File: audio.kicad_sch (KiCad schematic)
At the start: 100 parts, among them CN1 LEFT_JOY, CN2 RIGHT_JOY, CN3 RIGHT, CN4 LEFT, Q301 2N3906, Q321 MPF102, Q331 MPF102, Q921 MMBFJ113, Q931 MMBFJ113, U14 LF347, U15 74LS157, U3 PAULA, U38 MC1488, U90 DT1042, U91 DT1042, U92 DT1042, U93 DT1042

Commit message: DRAM chips replaced with SIMM module
Added logic to decode 2MB chip + 1.5MB slow
Rewired trapdoor slot
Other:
- title: Rämixx500 -> Rämixx500_max
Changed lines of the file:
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@@
 	(paper "A3")
 	(title_block
-		(title "Rämixx500")
-		(date "2021-05-22")
-		(rev "1")
+		(title "Rämixx500_max")
+		(date "2026-03-13")
+		(rev "2")
 		(company "SukkoPera")
 		(comment 1 "PAULA PREFERS THE TRADITIONAL MODES")

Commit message: removed ESD diodes
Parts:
- removed U90, U91, U92, U93: DT1042, Raemixx500:TSOP-6_Handsolder, symbol DT1042:DT1042
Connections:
- no-connect marks 2 -> 0
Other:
- note removed: "EXTRA TVS DIODES FOR ESD PROTECTION"

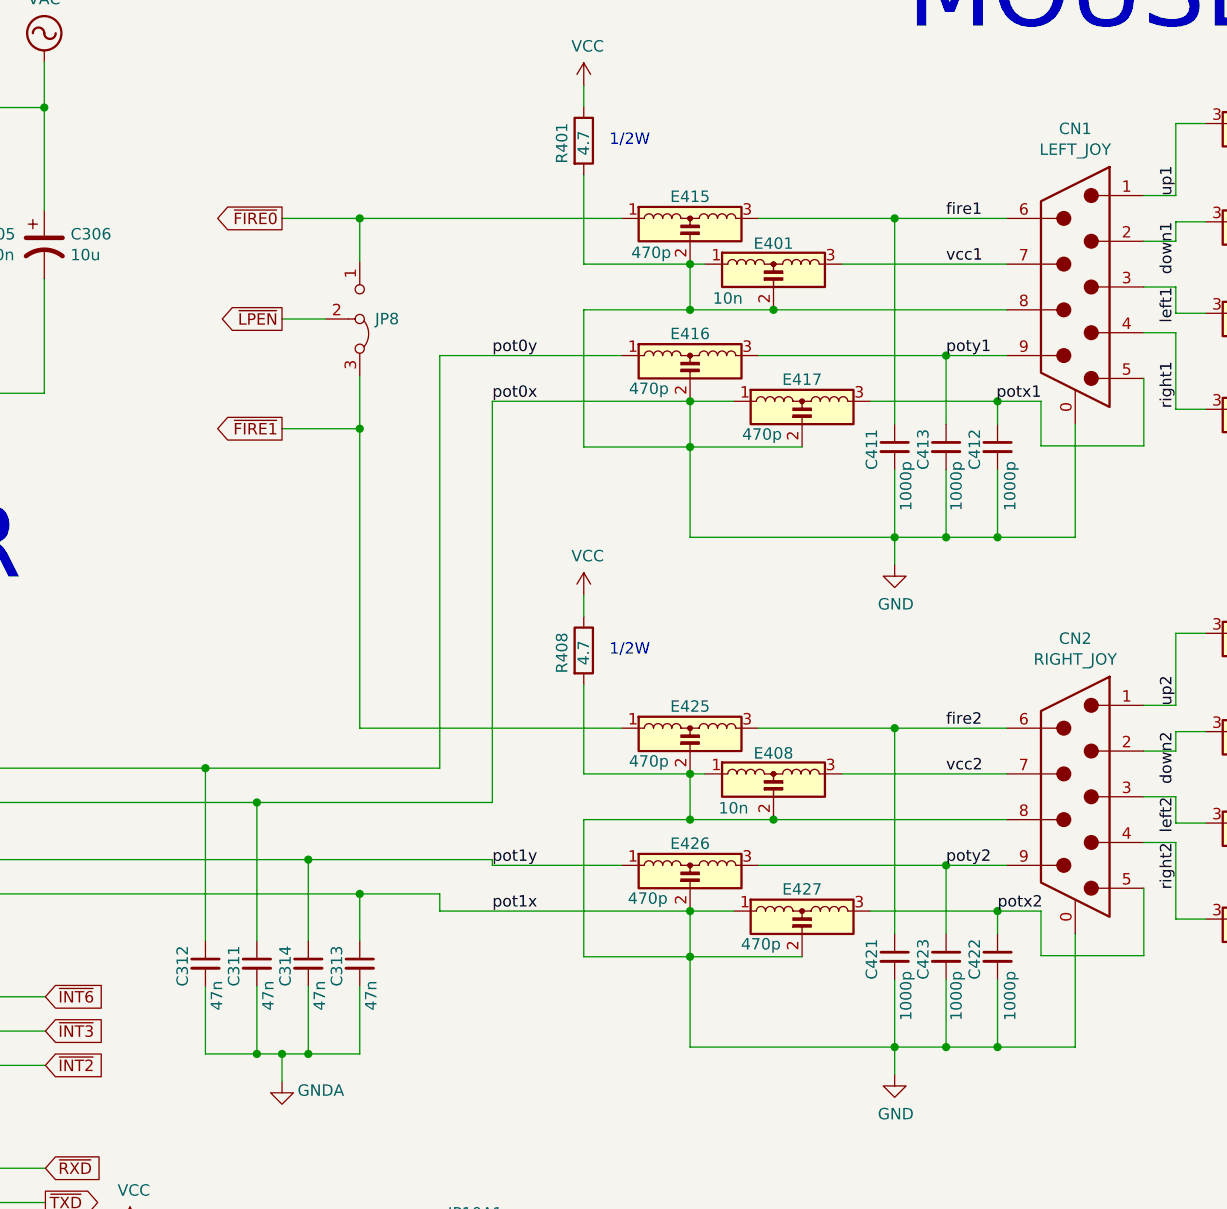
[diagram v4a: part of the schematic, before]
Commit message: Fixed some very nasty shorts that happened many commits ago when the design was imported into KiCad9.
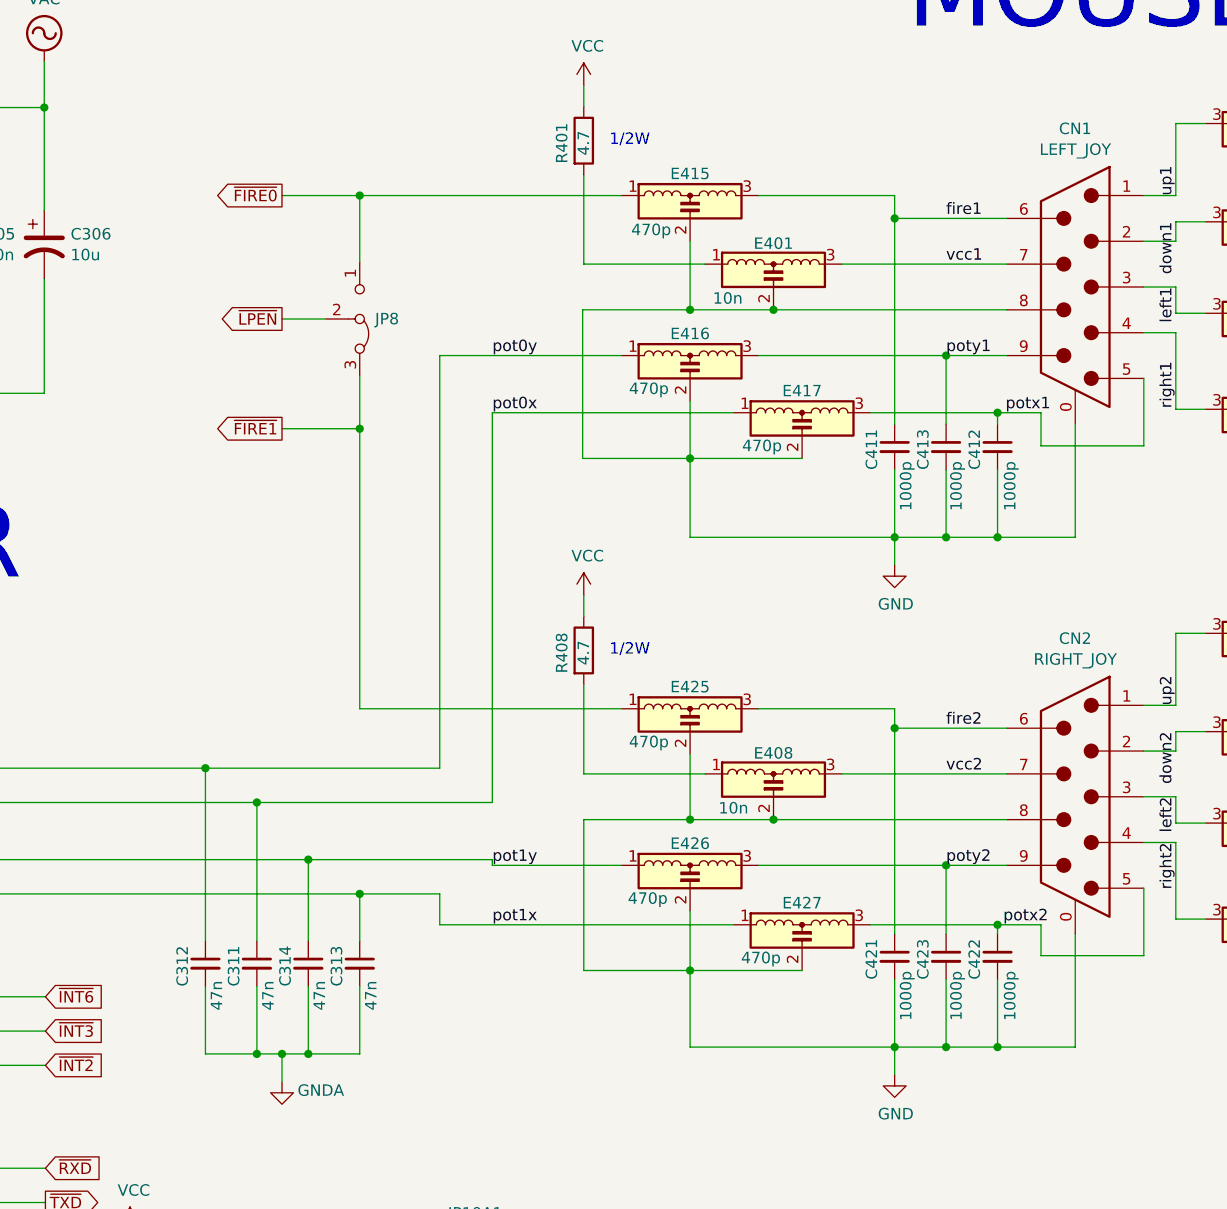
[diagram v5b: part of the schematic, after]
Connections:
- net GND: no longer C311.1, C313.1, E401.1, E408.1, E417.1, E427.1, R401.2, R408.2, U3.32 (P0X), U3.35 (P1X)
- new net: E401.1, R401.2
- new net: E408.1, R408.2
- new net pot0x: C311.1, E417.1, U3.32 (P0X)
- new net pot1x: C313.1, E427.1, U3.35 (P1X)
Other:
- moved on the sheet: E415, E417, E425, E427

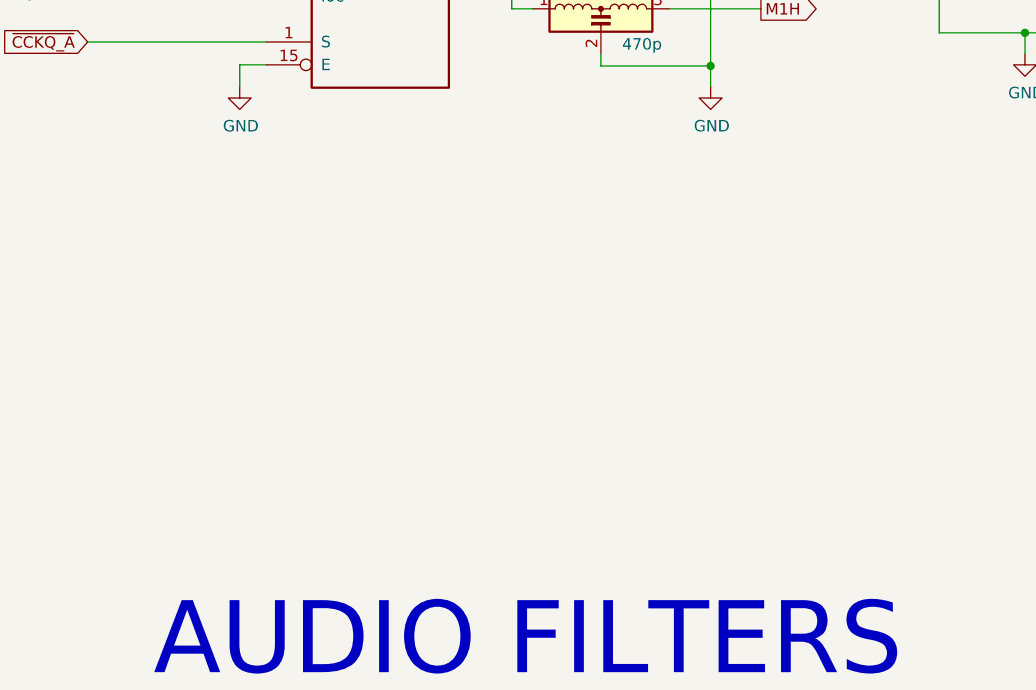
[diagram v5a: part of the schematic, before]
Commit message: Added back ESD diodes very close to sensitive pins only for more effective protection
Made teardrops as small as possible
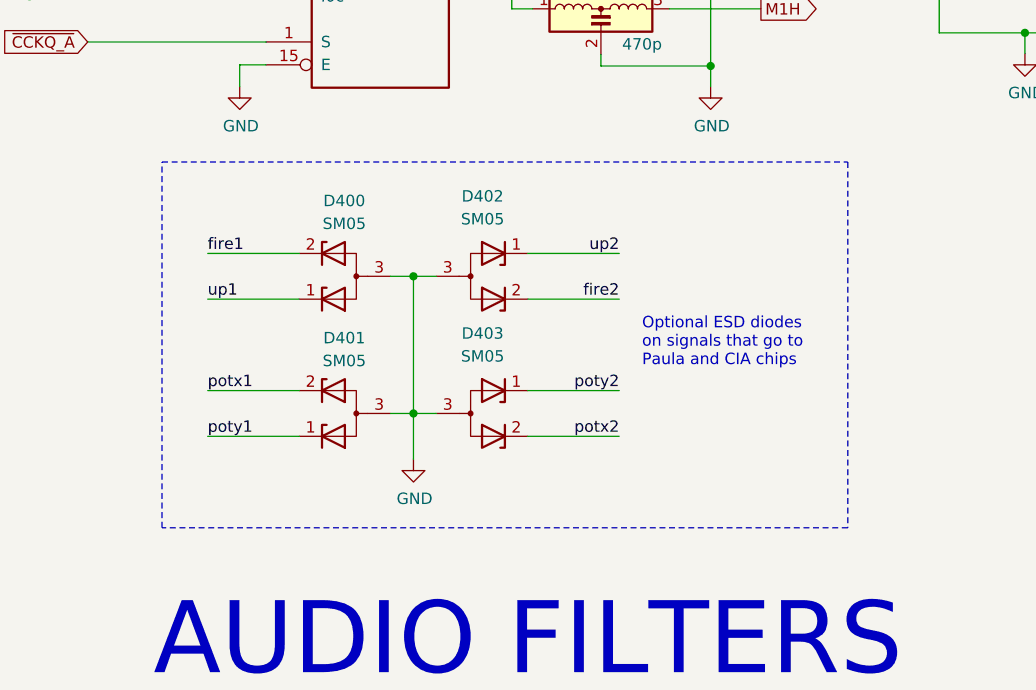
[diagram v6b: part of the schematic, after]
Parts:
- added D400, D401, D402, D403: SM05, Raemixx500:SOT-23_Handsoldering_NoSilk, symbol Device:D_Zener_Dual_CommonAnode_KKA_Parallel
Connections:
- net GND: now also D400.3 (A), D401.3 (A), D402.3 (A), D403.3 (A)
- net fire1: now also D400.2 (K)
- net fire2: now also D402.2 (K)
- net potx1: now also D401.2 (K)
- net potx2: now also D403.2 (K)
- net poty1: now also D401.1 (K)
- net poty2: now also D403.1 (K)
- net up1: now also D400.1 (K)
- net up2: now also D402.1 (K)
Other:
- note added: "Optional ESD diodes on signals that go to Paula and CIA chips"

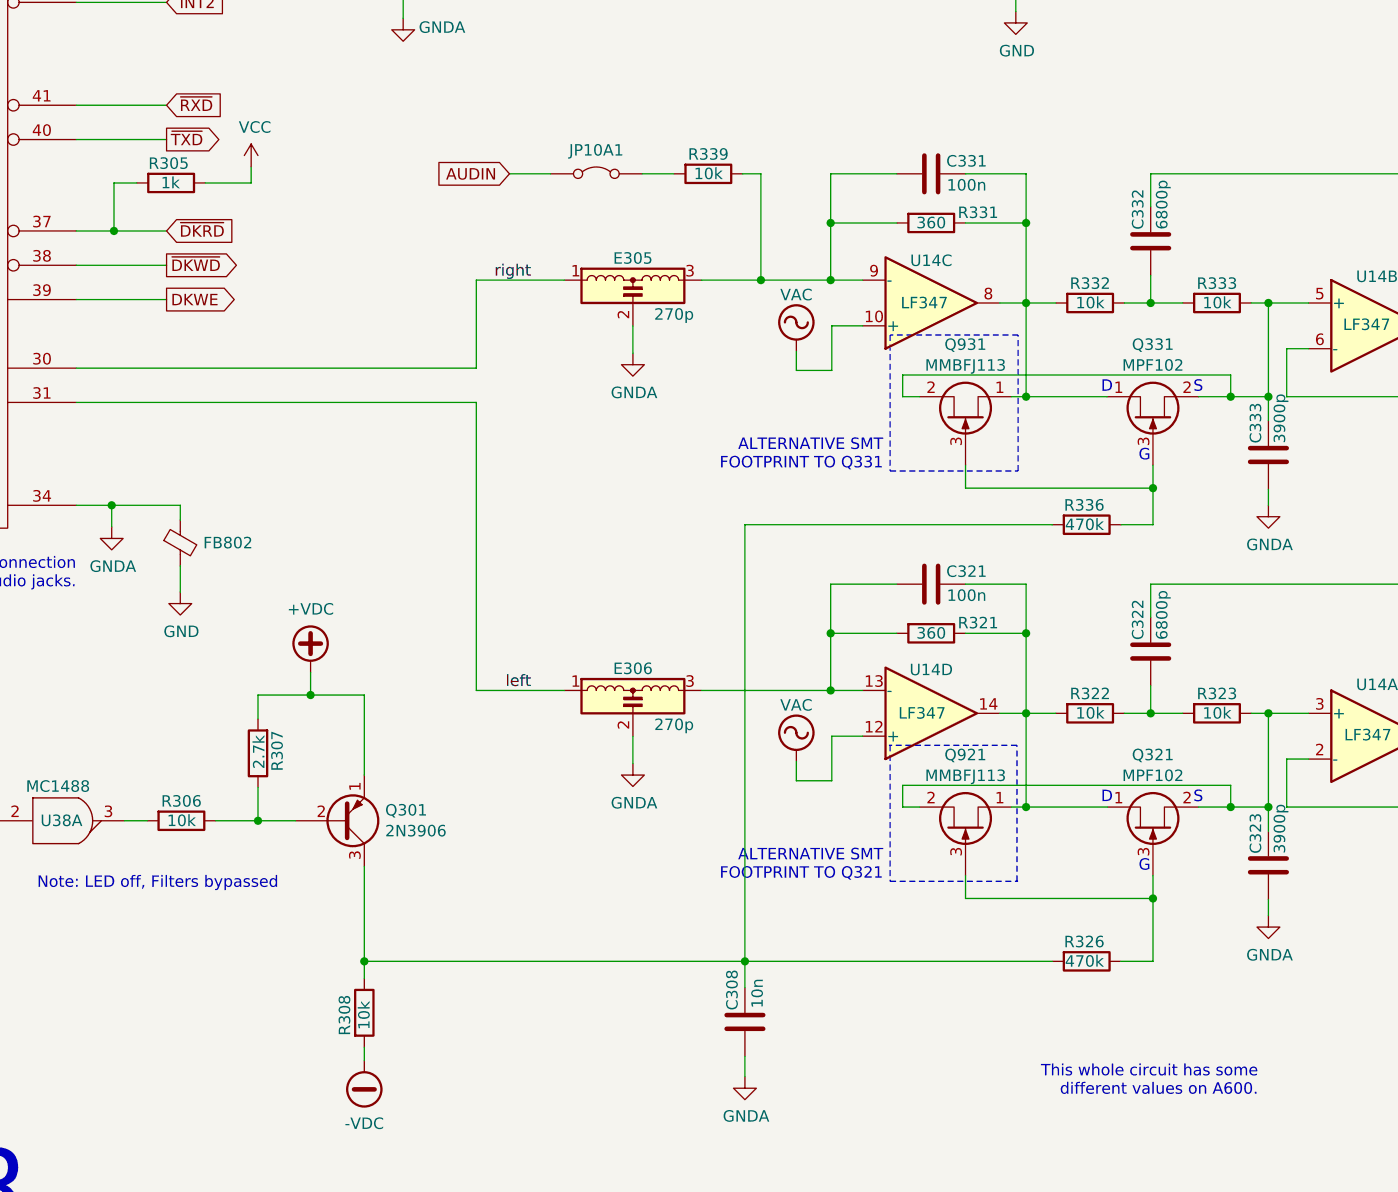
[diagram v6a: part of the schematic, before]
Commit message: Started cleaning up BOM
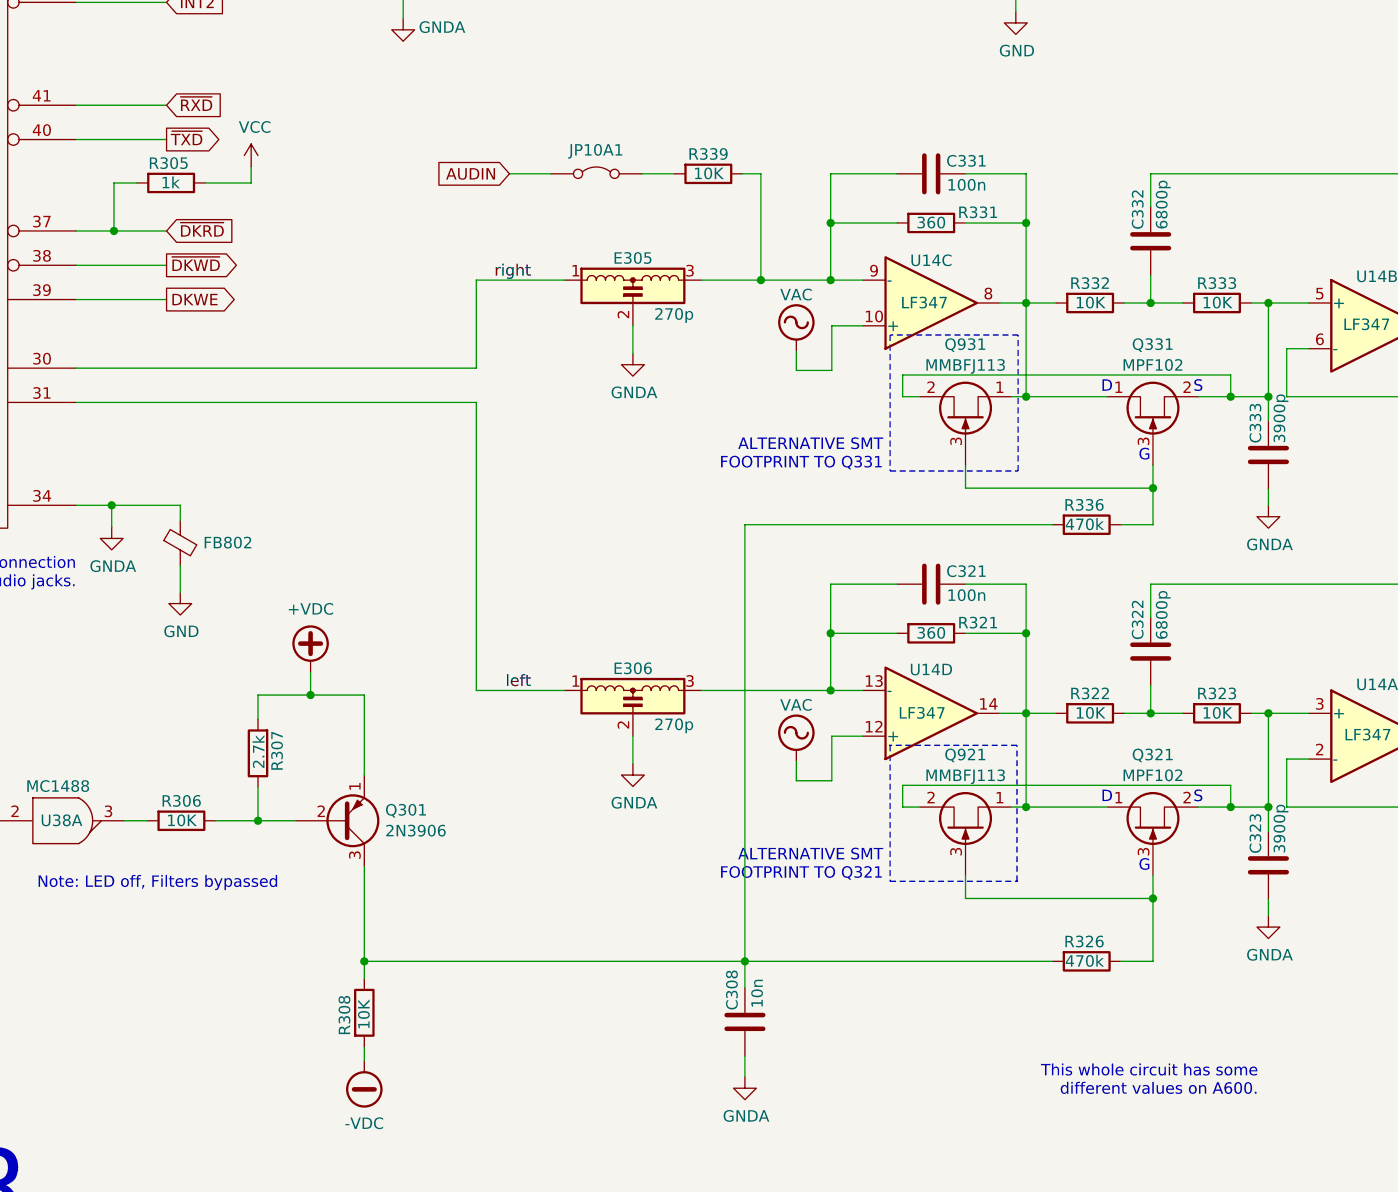
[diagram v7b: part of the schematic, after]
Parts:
- JP10A1, JP10B1, JP8: now left out of the parts list
- R306, R308, R322, R323, R332, R333, R339: value 10k -> 10K
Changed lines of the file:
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@@
 		(unit 1)
 		(exclude_from_sim no)
-		(in_bom yes)
+		(in_bom no)
 		(on_board yes)
 		(dnp no)
@@
 			)
 		)
-		(property "Value" "10k"
+		(property "Value" "10K"
 			(at 211.074 223.901 90)
 			(effects
@@
 			)
 		)
-		(property "Value" "10k"
+		(property "Value" "10K"
 			(at 225.171 223.901 90)
 			(effects
@@
 			)
 		)
-		(property "Value" "10k"
+		(property "Value" "10K"
 			(at 211.074 178.308 90)
 			(effects
@@
 			)
 		)
-		(property "Value" "10k"
+		(property "Value" "10K"
 			(at 225.171 178.308 90)
 			(effects
@@
 			)
 		)
-		(property "Value" "10k"
+		(property "Value" "10K"
 			(at 130.429 259.08 90)
 			(effects
@@
 			)
 		)
-		(property "Value" "10k"
+		(property "Value" "10K"
 			(at 110.109 235.839 90)
 			(effects
@@
 		(unit 1)
 		(exclude_from_sim no)
-		(in_bom yes)
+		(in_bom no)
 		(on_board yes)
 		(dnp no)
@@
 		(unit 1)
 		(exclude_from_sim no)
-		(in_bom yes)
+		(in_bom no)
 		(on_board yes)
 		(dnp no)
@@
 			)
 		)
-		(property "Value" "10k"
+		(property "Value" "10K"
 			(at 168.656 163.957 90)
 			(effects

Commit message: Working on BOM
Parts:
- C15, C308: MFG Part Num C410C103K1H5TAAUTO -> C410C103K1R5TA; Mouser (none) -> 80-C410C103K1R
- C3, C301, C302, C305, C325, C335: MFG Part Num C412C334M5U5TA -> C440C334K5R5TA7200; Mouser (none) -> 80-C440C334K5R-TR
- C303, C304: MFG Part Num EEUFR1H220 -> ECA-1EM220I; Mouser (none) -> 667-ECA-1EM220I
- C306: MFG Part Num EEUFR1H100 -> ECA-1EM100I; Mouser (none) -> 667-ECA-1EM100I
- C307: MFG Part Num EEUFR1C102 -> ECA-1EM102; Mouser (none) -> 667-ECA-1EM102
- C311, C312, C313, C314: MFG Part Num C410C473M5U5TA -> C410C473M5R5TA7200; Mouser (none) -> 80-C410C473M5R-TR
- C321, C331: MFG Name AVX -> VISHAY; MFG Part Num SA115C104KAR -> A104K15X7RF5TAA; Mouser (none) -> 594-A104K15X7RF5TAA
- C322, C332: MFG Part Num C430C682J5G5TA -> C410C682K2R5TA7200; Mouser (none) -> 80-C410C682K2R5TATU
- C323, C333: MFG Name N/A -> KEMET; MFG Part Num (none) -> C410C392K1R5TA; Mouser (none) -> 80-C410C392K1R
- C324, C334: MFG Part Num EEUFR1H220 -> ECA-1EM220B; Mouser (none) -> 667-ECA-1EM220B
- C411, C412, C413, C421, C422, C423: MFG Name AVX -> KEMET; MFG Part Num SA101C102KAR -> C410C102M5R5TA7200; Mouser (none) -> 80-C410C102M5R-TR
- CN1, CN2: MFG Name (none) -> AMPHENOL; MFG Part Num (none) -> L17HTNEP4F1C; Mouser (none) -> 523-L17HTNEP4F1C
- CN3, CN4: MFG Name (none) -> SWITCHCRAFT; MFG Part Num (none) -> PJRAN1X1U01AUX; Mouser (none) -> 502-PJRAN1X1U01AUX
